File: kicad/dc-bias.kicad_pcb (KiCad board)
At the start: 2 copper layers, 0 parts

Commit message: rough draft 6x4
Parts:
- added A1: Arduino_UNO_R3, Module:Arduino_UNO_R3, F.Cu at (189.2, 80.3)
- added J1: Conn_01x10, Connector_IDC:IDC-Header_2x05_P2.54mm_Vertical, F.Cu at (71.1, 144.8)
- added J2: Conn_01x10, Connector_IDC:IDC-Header_2x05_P2.54mm_Vertical, F.Cu at (121.9, 144.8)
- added REF**: MountingHole_3.2mm_M3, MountingHole:MountingHole_3.2mm_M3, F.Cu at (198.1, 147.3)
- added REF**: MountingHole_3.2mm_M3, MountingHole:MountingHole_3.2mm_M3, F.Cu at (198.1, 55.9)
- added REF**: MountingHole_3.2mm_M3, MountingHole:MountingHole_3.2mm_M3, F.Cu at (55.9, 55.9)
- added REF**: MountingHole_3.2mm_M3, MountingHole:MountingHole_3.2mm_M3, F.Cu at (55.9, 147.3)
- added U1: ~, Package_SO:SOIC-8-1EP_3.9x4.9mm_P1.27mm_EP2.95x4.9mm_Mask2.71x3.4mm_ThermalVias, F.Cu at (65.4, 88.3)
- added U10: ~, Package_SO:SOIC-8-1EP_3.9x4.9mm_P1.27mm_EP2.95x4.9mm_Mask2.71x3.4mm_ThermalVias, F.Cu at (182.4, 126.7)
- added U11: ~, Package_SO:SOIC-8-1EP_3.9x4.9mm_P1.27mm_EP2.95x4.9mm_Mask2.71x3.4mm_ThermalVias, F.Cu at (161.5, 109.5)
- added U12: ~, Package_SO:SOIC-8-1EP_3.9x4.9mm_P1.27mm_EP2.95x4.9mm_Mask2.71x3.4mm_ThermalVias, F.Cu at (161.5, 126.7)
- added U13: ~, Package_SO:SOIC-8-1EP_3.9x4.9mm_P1.27mm_EP2.95x4.9mm_Mask2.71x3.4mm_ThermalVias, F.Cu at (171.9, 109.5)
- added U14: ~, Package_SO:SOIC-8-1EP_3.9x4.9mm_P1.27mm_EP2.95x4.9mm_Mask2.71x3.4mm_ThermalVias, F.Cu at (151.0, 118.1)
- added U15: ~, Package_SO:SOIC-8-1EP_3.9x4.9mm_P1.27mm_EP2.95x4.9mm_Mask2.71x3.4mm_ThermalVias, F.Cu at (171.9, 118.1)
- added U16: ~, Package_SO:SOIC-8-1EP_3.9x4.9mm_P1.27mm_EP2.95x4.9mm_Mask2.71x3.4mm_ThermalVias, F.Cu at (161.5, 135.3)
- added U2: ~, Package_SO:SOIC-8-1EP_3.9x4.9mm_P1.27mm_EP2.95x4.9mm_Mask2.71x3.4mm_ThermalVias, F.Cu at (78.7, 89.5)
- added U3: ~, Package_SO:SOIC-8-1EP_3.9x4.9mm_P1.27mm_EP2.95x4.9mm_Mask2.71x3.4mm_ThermalVias, F.Cu at (67.9, 108.4)
- added U4: ~, Package_SO:SOIC-8-1EP_3.9x4.9mm_P1.27mm_EP2.95x4.9mm_Mask2.71x3.4mm_ThermalVias, F.Cu at (68.6, 119.4)
- added U5: ~, Package_SO:SOIC-8-1EP_3.9x4.9mm_P1.27mm_EP2.95x4.9mm_Mask2.71x3.4mm_ThermalVias, F.Cu at (85.7, 103.5)
- added U6: ~, Package_SO:SOIC-8-1EP_3.9x4.9mm_P1.27mm_EP2.95x4.9mm_Mask2.71x3.4mm_ThermalVias, F.Cu at (61.6, 130.4)
- added U7: ~, Package_SO:SOIC-8-1EP_3.9x4.9mm_P1.27mm_EP2.95x4.9mm_Mask2.71x3.4mm_ThermalVias, F.Cu at (88.2, 122.8)
- added U8: ~, Package_SO:SOIC-8-1EP_3.9x4.9mm_P1.27mm_EP2.95x4.9mm_Mask2.71x3.4mm_ThermalVias, F.Cu at (93.3, 87.0)
- added U9: ~, Package_SO:SOIC-8-1EP_3.9x4.9mm_P1.27mm_EP2.95x4.9mm_Mask2.71x3.4mm_ThermalVias, F.Cu at (161.5, 118.1)
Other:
- board outline added: 152.4 x 101.6 mm

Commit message: arduino, powersupply, dac
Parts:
- removed the REF** at (198.1, 147.3)
- removed the REF** at (198.1, 55.9)
- removed the REF** at (55.9, 55.9)
- removed the REF** at (55.9, 147.3)
- added J7: OQ0271010000G, SamacSys_Parts:OQ0271010000G, F.Cu at (184.7, 40.8)
- added REF**: MountingHole_3.2mm_M3, MountingHole:MountingHole_3.2mm_M3, F.Cu at (200.0, 133.3)
- added REF**: MountingHole_3.2mm_M3, MountingHole:MountingHole_3.2mm_M3, F.Cu at (53.9, 44.5)
- added REF**: MountingHole_3.2mm_M3, MountingHole:MountingHole_3.2mm_M3, F.Cu at (53.9, 133.3)
- added REF**: MountingHole_3.2mm_M3, MountingHole:MountingHole_3.2mm_M3, F.Cu at (200.0, 44.5)
- added U17: ~, footprints:VHB75W, B.Cu at (152.4, 76.2)
- added U18: DAC, footprints:adafruitDAC7578, F.Cu at (19.1, 100.2)
- added U19: DAC, footprints:adafruitDAC7578, F.Cu at (16.8, 125.7)
- A1: value Arduino_UNO_R3 -> Arduino R4 Minima; footprint Module:Arduino_UNO_R3 -> footprints:Arduino_Uno_R4_Minima_Shield
- moved U6 316.5 mm to (365.7, 42.6)
- moved U4 304.9 mm to (365.7, 51.1)
- moved U5 288.5 mm to (365.7, 34.0)
- moved U8 281.3 mm to (365.7, 16.8)
- moved U1 270.7 mm to (336.1, 89.5)
- moved U2 267.9 mm to (346.5, 80.9)
- moved U3 258.4 mm to (325.6, 89.5)
- moved U7 241.1 mm to (325.6, 80.9)
- moved U16 214.9 mm to (365.7, 68.3)
- moved U10 209.4 mm to (365.7, 25.4)
- moved U15 202.4 mm to (365.7, 59.7)
- moved U14 188.7 mm to (336.1, 80.9)
- moved U11 155.0 mm to (315.2, 89.5)
- moved U12 150.4 mm to (304.7, 80.9)
- moved U13 146.0 mm to (315.2, 80.9)
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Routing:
- added copper zone on B.Cu, net GND
- added copper zone on F.Cu, net GND
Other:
- board size 152.4 x 101.6 mm -> 158.8 x 101.6 mm

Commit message: unlock
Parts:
- moved U19 67.8 mm to (73.2, 88.0)
- moved U18 62.7 mm to (73.0, 68.2)

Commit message: finished schematic
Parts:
- removed J7: OQ0271010000G, SamacSys_Parts:OQ0271010000G
- added C1: 100u, Capacitor_THT:CP_Radial_D7.5mm_P2.50mm, F.Cu at (265.6, 64.0)
- added C2: 100u, Capacitor_THT:CP_Radial_D7.5mm_P2.50mm, F.Cu at (265.6, 73.0)
- added D1: LED, LED_SMD:LED_1206_3216Metric_Pad1.42x1.75mm_HandSolder, F.Cu at (274.4, 73.7)
- added D2: LED, LED_SMD:LED_1206_3216Metric_Pad1.42x1.75mm_HandSolder, F.Cu at (274.4, 77.1)
- added J2: Conn_01x10, Connector_IDC:IDC-Header_2x05_P2.54mm_Vertical, F.Cu at (224.4, 65.6)
- added J3: 24V_IN, TerminalBlock_CUI:TerminalBlock_CUI_TB007-508-02_1x02_P5.08mm_Horizontal, F.Cu at (275.0, 65.4)
- added J4: Conn_01x10, Connector_IDC:IDC-Header_2x05_P2.54mm_Vertical, F.Cu at (224.4, 41.2)
- added R1: 2k2, Resistor_SMD:R_1206_3216Metric_Pad1.30x1.75mm_HandSolder, F.Cu at (280.4, 73.7)
- added R2: 2k2, Resistor_SMD:R_1206_3216Metric_Pad1.30x1.75mm_HandSolder, F.Cu at (280.4, 77.0)
- added R33: 10k, Resistor_SMD:R_1206_3216Metric_Pad1.30x1.75mm_HandSolder, F.Cu at (243.1, 107.3)
- added R34: 82k, Resistor_SMD:R_1206_3216Metric_Pad1.30x1.75mm_HandSolder, F.Cu at (243.1, 110.6)
- added R35: 10k, Resistor_SMD:R_1206_3216Metric_Pad1.30x1.75mm_HandSolder, F.Cu at (284.9, 107.3)
- added R36: 82k, Resistor_SMD:R_1206_3216Metric_Pad1.30x1.75mm_HandSolder, F.Cu at (284.9, 110.6)
- added R37: 10k, Resistor_SMD:R_1206_3216Metric_Pad1.30x1.75mm_HandSolder, F.Cu at (222.2, 107.3)
- added R38: 82k, Resistor_SMD:R_1206_3216Metric_Pad1.30x1.75mm_HandSolder, F.Cu at (222.2, 110.6)
- added R39: 10k, Resistor_SMD:R_1206_3216Metric_Pad1.30x1.75mm_HandSolder, F.Cu at (264.0, 107.3)
- added R40: 82k, Resistor_SMD:R_1206_3216Metric_Pad1.30x1.75mm_HandSolder, F.Cu at (264.0, 110.6)
- added R41: 10k, Resistor_SMD:R_1206_3216Metric_Pad1.30x1.75mm_HandSolder, F.Cu at (232.6, 107.3)
- added R42: 82k, Resistor_SMD:R_1206_3216Metric_Pad1.30x1.75mm_HandSolder, F.Cu at (232.6, 110.6)
- added R43: 10k, Resistor_SMD:R_1206_3216Metric_Pad1.30x1.75mm_HandSolder, F.Cu at (284.9, 92.1)
- added R44: 82k, Resistor_SMD:R_1206_3216Metric_Pad1.30x1.75mm_HandSolder, F.Cu at (284.9, 95.4)
- added R45: 10k, Resistor_SMD:R_1206_3216Metric_Pad1.30x1.75mm_HandSolder, F.Cu at (253.5, 92.1)
- added R46: 82k, Resistor_SMD:R_1206_3216Metric_Pad1.30x1.75mm_HandSolder, F.Cu at (253.5, 95.4)
- added R47: 10k, Resistor_SMD:R_1206_3216Metric_Pad1.30x1.75mm_HandSolder, F.Cu at (265.2, 43.3)
- added R48: 82k, Resistor_SMD:R_1206_3216Metric_Pad1.30x1.75mm_HandSolder, F.Cu at (265.2, 46.6)
- added R49: 10k, Resistor_SMD:R_1206_3216Metric_Pad1.30x1.75mm_HandSolder, F.Cu at (253.5, 107.3)
- added R50: 82k, Resistor_SMD:R_1206_3216Metric_Pad1.30x1.75mm_HandSolder, F.Cu at (253.5, 110.6)
- added R51: 10k, Resistor_SMD:R_1206_3216Metric_Pad1.30x1.75mm_HandSolder, F.Cu at (275.6, 43.3)
- added R52: 82k, Resistor_SMD:R_1206_3216Metric_Pad1.30x1.75mm_HandSolder, F.Cu at (275.6, 46.6)
- added R53: 10k, Resistor_SMD:R_1206_3216Metric_Pad1.30x1.75mm_HandSolder, F.Cu at (232.6, 92.1)
- added R54: 82k, Resistor_SMD:R_1206_3216Metric_Pad1.30x1.75mm_HandSolder, F.Cu at (232.6, 95.4)
- added R55: 10k, Resistor_SMD:R_1206_3216Metric_Pad1.30x1.75mm_HandSolder, F.Cu at (274.4, 92.1)
- added R56: 82k, Resistor_SMD:R_1206_3216Metric_Pad1.30x1.75mm_HandSolder, F.Cu at (274.4, 95.4)
- added R57: 10k, Resistor_SMD:R_1206_3216Metric_Pad1.30x1.75mm_HandSolder, F.Cu at (222.2, 92.1)
- added R58: 82k, Resistor_SMD:R_1206_3216Metric_Pad1.30x1.75mm_HandSolder, F.Cu at (222.2, 95.4)
- added R59: 10k, Resistor_SMD:R_1206_3216Metric_Pad1.30x1.75mm_HandSolder, F.Cu at (264.0, 92.1)
- added R60: 82k, Resistor_SMD:R_1206_3216Metric_Pad1.30x1.75mm_HandSolder, F.Cu at (264.0, 95.4)
- added R61: 10k, Resistor_SMD:R_1206_3216Metric_Pad1.30x1.75mm_HandSolder, F.Cu at (243.1, 92.1)
- added R62: 82k, Resistor_SMD:R_1206_3216Metric_Pad1.30x1.75mm_HandSolder, F.Cu at (243.1, 95.4)
- added R63: 10k, Resistor_SMD:R_1206_3216Metric_Pad1.30x1.75mm_HandSolder, F.Cu at (274.4, 107.3)
- added R64: 82k, Resistor_SMD:R_1206_3216Metric_Pad1.30x1.75mm_HandSolder, F.Cu at (274.4, 110.6)
- added U19: DAC, footprints:adafruitDAC7578, F.Cu at (234.3, 77.8)
- added U20: ~, Package_SO:SOIC-8-1EP_3.9x4.9mm_P1.27mm_EP2.95x4.9mm_Mask2.71x3.4mm_ThermalVias, F.Cu at (244.3, 102.4)
- added U21: DAC, footprints:adafruitDAC7578, F.Cu at (234.3, 53.4)
- added U22: ~, Package_SO:SOIC-8-1EP_3.9x4.9mm_P1.27mm_EP2.95x4.9mm_Mask2.71x3.4mm_ThermalVias, F.Cu at (286.1, 102.4)
- added U23: ~, Package_SO:SOIC-8-1EP_3.9x4.9mm_P1.27mm_EP2.95x4.9mm_Mask2.71x3.4mm_ThermalVias, F.Cu at (223.4, 102.4)
- added U24: ~, Package_SO:SOIC-8-1EP_3.9x4.9mm_P1.27mm_EP2.95x4.9mm_Mask2.71x3.4mm_ThermalVias, F.Cu at (265.2, 102.4)
- added U25: ~, Package_SO:SOIC-8-1EP_3.9x4.9mm_P1.27mm_EP2.95x4.9mm_Mask2.71x3.4mm_ThermalVias, F.Cu at (233.9, 102.4)
- added U26: ~, Package_SO:SOIC-8-1EP_3.9x4.9mm_P1.27mm_EP2.95x4.9mm_Mask2.71x3.4mm_ThermalVias, F.Cu at (286.1, 87.2)
- added U27: ~, Package_SO:SOIC-8-1EP_3.9x4.9mm_P1.27mm_EP2.95x4.9mm_Mask2.71x3.4mm_ThermalVias, F.Cu at (254.8, 87.2)
- added U28: ~, Package_SO:SOIC-8-1EP_3.9x4.9mm_P1.27mm_EP2.95x4.9mm_Mask2.71x3.4mm_ThermalVias, F.Cu at (266.4, 38.4)
- added U29: ~, Package_SO:SOIC-8-1EP_3.9x4.9mm_P1.27mm_EP2.95x4.9mm_Mask2.71x3.4mm_ThermalVias, F.Cu at (254.8, 102.4)
- added U30: ~, Package_SO:SOIC-8-1EP_3.9x4.9mm_P1.27mm_EP2.95x4.9mm_Mask2.71x3.4mm_ThermalVias, F.Cu at (276.9, 38.4)
- added U31: ~, Package_SO:SOIC-8-1EP_3.9x4.9mm_P1.27mm_EP2.95x4.9mm_Mask2.71x3.4mm_ThermalVias, F.Cu at (233.9, 87.2)
- added U32: ~, Package_SO:SOIC-8-1EP_3.9x4.9mm_P1.27mm_EP2.95x4.9mm_Mask2.71x3.4mm_ThermalVias, F.Cu at (275.7, 87.2)
- added U33: ~, Package_SO:SOIC-8-1EP_3.9x4.9mm_P1.27mm_EP2.95x4.9mm_Mask2.71x3.4mm_ThermalVias, F.Cu at (223.4, 87.2)
- added U34: ~, Package_SO:SOIC-8-1EP_3.9x4.9mm_P1.27mm_EP2.95x4.9mm_Mask2.71x3.4mm_ThermalVias, F.Cu at (265.2, 87.2)
- added U35: ~, Package_SO:SOIC-8-1EP_3.9x4.9mm_P1.27mm_EP2.95x4.9mm_Mask2.71x3.4mm_ThermalVias, F.Cu at (244.3, 87.2)
- added U36: ~, Package_SO:SOIC-8-1EP_3.9x4.9mm_P1.27mm_EP2.95x4.9mm_Mask2.71x3.4mm_ThermalVias, F.Cu at (275.7, 102.4)
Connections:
- A1 pad 3V3: unconnected-(A1-3.3V-Pad3V3) -> +3V3
- A1 pad 5V1: unconnected-(A1-5V-Pad5V1) -> +5V
- A1 pad GND1: unconnected-(A1-GND-PadGND1) -> GND
- A1 pad GND2: unconnected-(A1-GND-PadGND2) -> GND
- A1 pad GND3: unconnected-(A1-GND-PadGND3) -> GND
- A1 pad GND4: unconnected-(A1-SPI_GND-PadGND4) -> GND
- A1 pad SCL: unconnected-(A1-PadSCL) -> SCL
- A1 pad SDA: unconnected-(A1-PadSDA) -> SDA
- U17 pad 1: unconnected-(U17-+V_IN-Pad1) -> +24V
- U17 pad 3: unconnected-(U17-CASE-Pad3) -> GND
- U17 pad 4: unconnected-(U17--V_IN-Pad4) -> GND
- U17 pad 5: unconnected-(U17--V_OUT-Pad5) -> GND
- U17 pad 9: unconnected-(U17-+V_OUT-Pad9) -> +48V

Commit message: unlock again
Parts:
- removed J1: Conn_01x10, Connector_IDC:IDC-Header_2x05_P2.54mm_Vertical
- removed the J2 at (147.3, 134.1)
- removed U18: DAC, footprints:adafruitDAC7578
- removed the U19 at (73.2, 88.0)

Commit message: leds
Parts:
- moved R2 154.6 mm to (129.7, 42.0), turned to 180 degrees
- moved D2 143.1 mm to (135.7, 41.9), turned to 180 degrees
- moved R1 116.7 mm to (168.0, 42.0), turned to 180 degrees
- moved D1 105.3 mm to (174.0, 41.9), turned to 180 degrees
- moved J3 85.8 mm to (191.8, 44.5), turned to 180 degrees
- moved C1 75.4 mm to (190.5, 57.1)
- moved C2 75.2 mm to (190.5, 69.8)

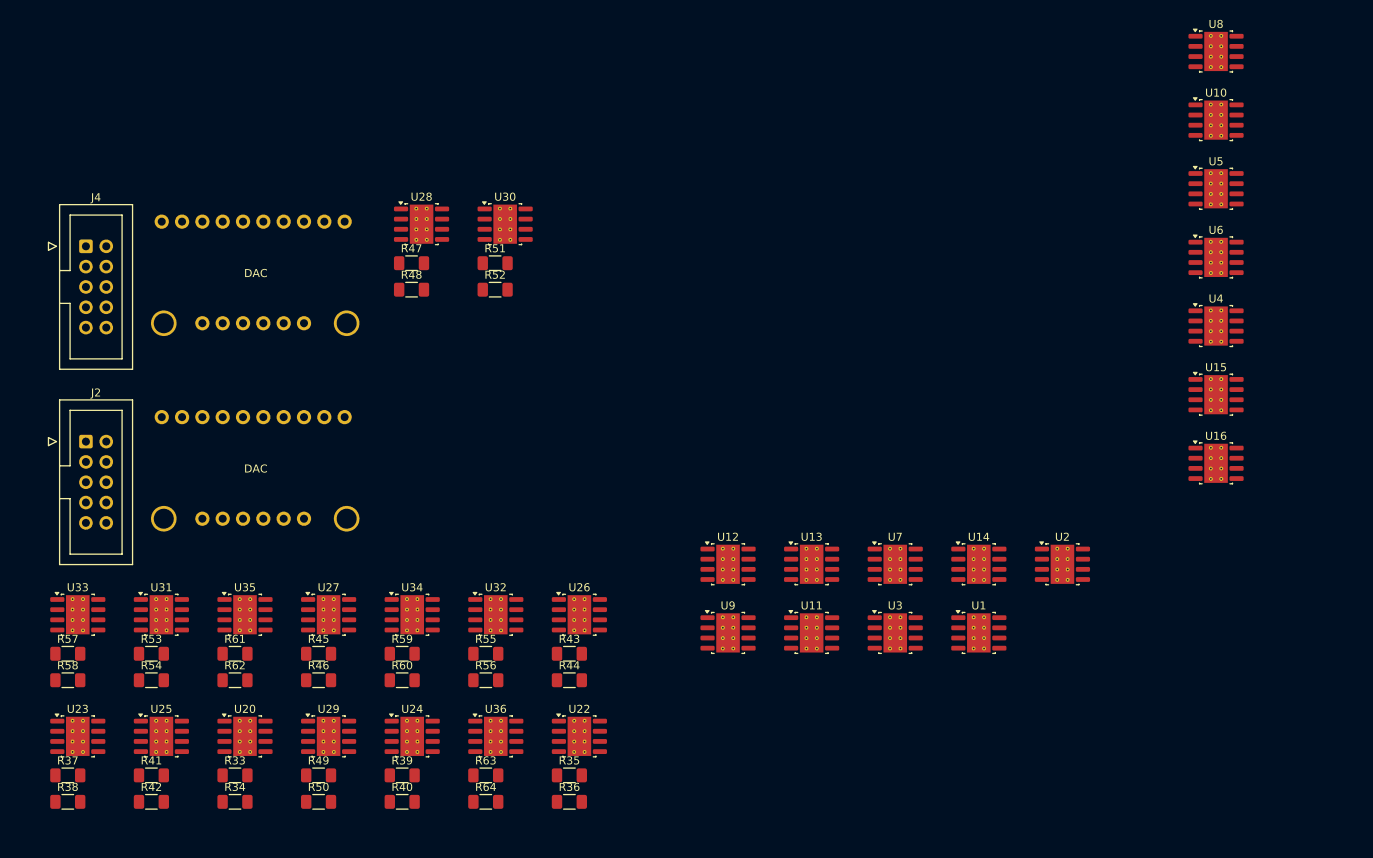
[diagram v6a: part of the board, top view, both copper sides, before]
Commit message: import from schematic
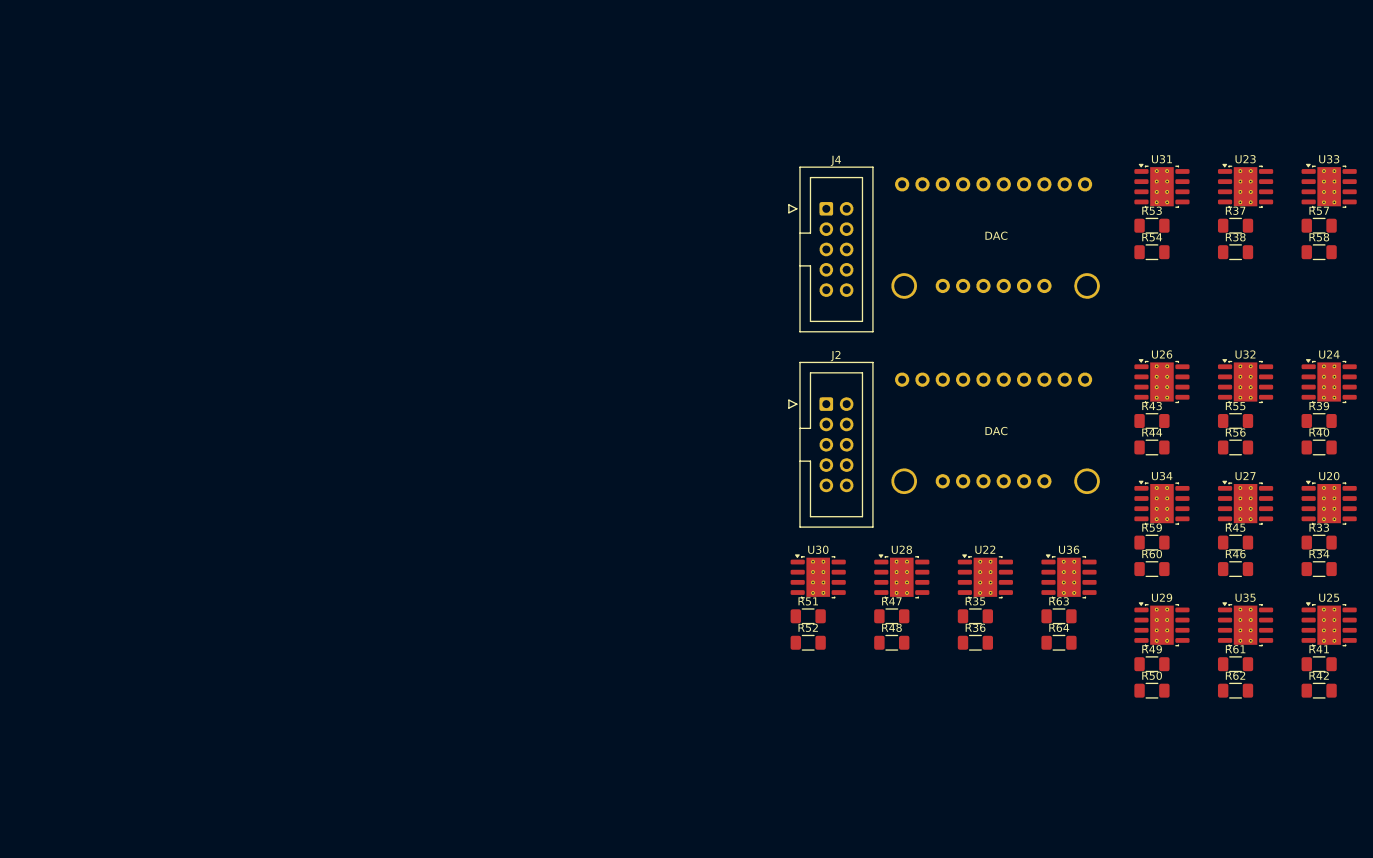
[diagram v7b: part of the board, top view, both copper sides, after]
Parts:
- removed U1, U10, U11, U12, U13, U14, U15, U16, U2, U3, U4, U5, U6, U7, U8, U9: ~, Package_SO:SOIC-8-1EP_3.9x4.9mm_P1.27mm_EP2.95x4.9mm_Mask2.71x3.4mm_ThermalVias
- moved R57 165.3 mm to (378.6, 38.6)
- moved R58 165.3 mm to (378.6, 41.9)
- moved U33 165.3 mm to (379.9, 33.7)
- moved R37 161.3 mm to (368.2, 38.6)
- moved R38 161.3 mm to (368.2, 41.9)
- moved U23 161.3 mm to (369.4, 33.7)
- moved R41 146.6 mm to (378.6, 93.4)
- moved R42 146.6 mm to (378.6, 96.7)
- moved U25 146.6 mm to (379.9, 88.5)
- moved R33 138.6 mm to (378.6, 78.2)
- moved R34 138.6 mm to (378.6, 81.5)
- moved U20 138.6 mm to (379.9, 73.3)
- moved R53 136.0 mm to (357.7, 38.6)
- moved R54 136.0 mm to (357.7, 41.9)
- moved U31 136.0 mm to (359.0, 33.7)
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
